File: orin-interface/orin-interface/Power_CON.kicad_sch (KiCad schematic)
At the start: 2 parts, among them J11 530470410, J16 530470410

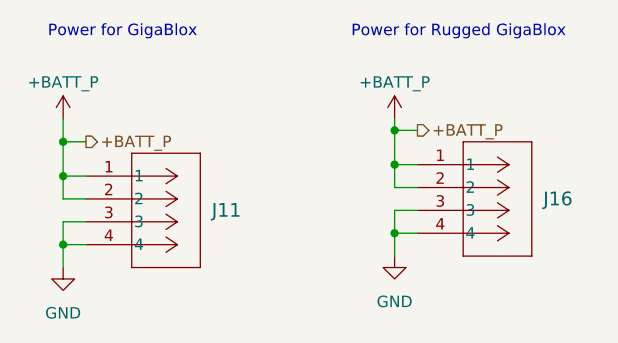
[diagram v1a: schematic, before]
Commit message: orin-interface: PoE channels, buses, 3V3 regulator, ERC fixes
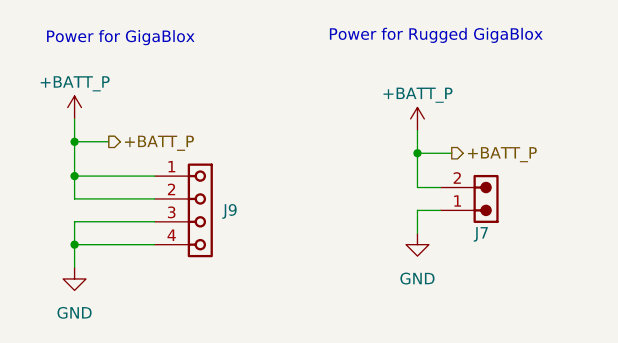
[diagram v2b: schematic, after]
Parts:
- removed J11, J16: 530470410, CONN04_530470410_MOL, symbol 530470410:530470410
- added J7: 64600211622, Connector_Wuerth:Wuerth_WR-WTB_64800211622_1x02_P1.50mm_Vertical, symbol Wurth_WR-WTB:64600211622
- added J9: 691101810004, 691378140024-2:J_Wurth_WR-TBL_691101810004, symbol WR-TBL Terminal Blocks:691101810004
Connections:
- net +BATT_P: now also J7.2, J9.1, J9.2
- net GND: now also J7.1, J9.3, J9.4

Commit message: orin-interface: add ETH connector sheets and Mate-connectors footprint lib; update orin-bob
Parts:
- removed J9: 691101810004, 691378140024-2:J_Wurth_WR-TBL_691101810004, symbol WR-TBL Terminal Blocks:691101810004
- added J11: 64600411622, Wurth_WR-WTB:J_Wurth_WR-WTB_64600411622, symbol WR-WTB:64600411622
- J7: footprint Connector_Wuerth:Wuerth_WR-WTB_64800211622_1x02_P1.50mm_Vertical -> Wurth_WR-WTB:J_Wurth_WR-WTB_64600211622
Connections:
- net +BATT_P: now also J11.3, J11.4
- net GND: now also J11.1, J11.2
